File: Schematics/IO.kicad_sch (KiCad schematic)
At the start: 1 part

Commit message: BOM + Motor Controllers
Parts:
- added R?: 0R, symbol Device:R_Small_US
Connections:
- net Earth: now also R?.2
- net at J?.4 (ID): now also R?.1
- no-connect marks 1 -> 0
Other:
- note added: "NL"
- moved on the sheet: J?
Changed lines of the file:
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@@
 (kicad_sch (version 20211123) (generator eeschema)
   (paper "A4")
-  (junction (at 64.135 73.66) (diameter 0) (color 0 0 0 0)
+  (junction (at 70.485 73.025) (diameter 0) (color 0 0 0 0)
   )
-  (no_connect (at 74.295 66.04))
-  (wire (pts (xy 74.295 55.88) (xy 81.28 55.88))
+  (wire (pts (xy 80.645 55.245) (xy 87.63 55.245))
     (stroke (width 0) (type default) (color 0 0 0 0))
   )
-  (wire (pts (xy 74.295 60.96) (xy 81.28 60.96))
+  (wire (pts (xy 80.645 65.405) (xy 83.82 65.405))
     (stroke (width 0) (type default) (color 0 0 0 0))
   )
-  (wire (pts (xy 64.135 73.66) (xy 64.135 71.12))
+  (wire (pts (xy 80.645 60.325) (xy 87.63 60.325))
     (stroke (width 0) (type default) (color 0 0 0 0))
   )
-  (wire (pts (xy 64.135 76.2) (xy 64.135 73.66))
+  (wire (pts (xy 70.485 73.025) (xy 70.485 70.485))
     (stroke (width 0) (type default) (color 0 0 0 0))
   )
-  (wire (pts (xy 64.135 73.66) (xy 66.675 73.66))
+  (wire (pts (xy 70.485 75.565) (xy 70.485 73.025))
     (stroke (width 0) (type default) (color 0 0 0 0))
   )
-  (wire (pts (xy 74.295 63.5) (xy 81.28 63.5))
+  (wire (pts (xy 83.82 73.66) (xy 83.82 75.565))
     (stroke (width 0) (type default) (color 0 0 0 0))
   )
-  (wire (pts (xy 66.675 73.66) (xy 66.675 71.12))
+  (wire (pts (xy 83.82 65.405) (xy 83.82 68.58))
     (stroke (width 0) (type default) (color 0 0 0 0))
   )
-  (global_label "D+" (shape input) (at 81.28 60.96 0) (fields_autoplaced)
+  (wire (pts (xy 70.485 73.025) (xy 73.025 73.025))
+    (stroke (width 0) (type default) (color 0 0 0 0))
+  )
+  (wire (pts (xy 80.645 62.865) (xy 87.63 62.865))
+    (stroke (width 0) (type default) (color 0 0 0 0))
+  )
+  (wire (pts (xy 73.025 73.025) (xy 73.025 70.485))
+    (stroke (width 0) (type default) (color 0 0 0 0))
+  )
+  (text "NL" (at 86.36 75.565 0)
+    (effects (font (size 1.27 1.27)) (justify left bottom))
+  )
+  (global_label "D+" (shape input) (at 87.63 60.325 0) (fields_autoplaced)
     (effects (font (size 1.27 1.27)) (justify left))
-    (property "Intersheet References" "${INTERSHEET_REFS}" (id 0) (at 86.5355 60.8806 0)
+    (property "Intersheet References" "${INTERSHEET_REFS}" (id 0) (at 92.8855 60.2456 0)
       (effects (font (size 1.27 1.27)) (justify left) hide)
     )
   )
-  (global_label "VBUS" (shape input) (at 81.28 55.88 0) (fields_autoplaced)
+  (global_label "VBUS" (shape input) (at 87.63 55.245 0) (fields_autoplaced)
     (effects (font (size 1.27 1.27)) (justify left))
-    (property "Intersheet References" "${INTERSHEET_REFS}" (id 0) (at 88.5917 55.8006 0)
+    (property "Intersheet References" "${INTERSHEET_REFS}" (id 0) (at 94.9417 55.1656 0)
       (effects (font (size 1.27 1.27)) (justify left) hide)
     )
   )
-  (global_label "D-" (shape input) (at 81.28 63.5 0) (fields_autoplaced)
+  (global_label "D-" (shape input) (at 87.63 62.865 0) (fields_autoplaced)
     (effects (font (size 1.27 1.27)) (justify left))
-    (property "Intersheet References" "${INTERSHEET_REFS}" (id 0) (at 86.5355 63.4206 0)
+    (property "Intersheet References" "${INTERSHEET_REFS}" (id 0) (at 92.8855 62.7856 0)
       (effects (font (size 1.27 1.27)) (justify left) hide)
     )
   )
-  (symbol (lib_id "Connector:USB_B_Micro") (at 66.675 60.96 0) (unit 1)
+  (symbol (lib_id "Device:R_Small_US") (at 83.82 71.12 0) (unit 1)
     (in_bom yes) (on_board yes) (fields_autoplaced)
-    (property "Reference" "J?" (id 0) (at 66.675 48.26 0))
-    (property "Value" "USB_B_Micro" (id 1) (at 66.675 50.8 0))
-    (property "Footprint" "" (id 2) (at 70.485 62.23 0)
+    (property "Reference" "R?" (id 0) (at 86.36 69.8499 0)
+      (effects (font (size 1.27 1.27)) (justify left))
+    )
+    (property "Value" "0R" (id 1) (at 86.36 72.3899 0)
+      (effects (font (size 1.27 1.27)) (justify left))
+    )
+    (property "Footprint" "" (id 2) (at 83.82 71.12 0)
       (effects (font (size 1.27 1.27)) hide)
     )
-    (property "Datasheet" "~" (id 3) (at 70.485 62.23 0)
+    (property "Datasheet" "~" (id 3) (at 83.82 71.12 0)
+      (effects (font (size 1.27 1.27)) hide)
+    )
+    (pin "1")
+    (pin "2")
+  )
+  (symbol (lib_id "power:Earth") (at 83.82 75.565 0) (unit 1)
+    (in_bom yes) (on_board yes) (fields_autoplaced)
+    (property "Reference" "#PWR?" (id 0) (at 83.82 81.915 0)
+      (effects (font (size 1.27 1.27)) hide)
+    )
+    (property "Value" "Earth" (id 1) (at 83.82 79.375 0)
+      (effects (font (size 1.27 1.27)) hide)
+    )
+    (property "Footprint" "" (id 2) (at 83.82 75.565 0)
+      (effects (font (size 1.27 1.27)) hide)
+    )
+    (property "Datasheet" "~" (id 3) (at 83.82 75.565 0)
+      (effects (font (size 1.27 1.27)) hide)
+    )
+    (pin "1")
+  )
+  (symbol (lib_id "Connector:USB_B_Micro") (at 73.025 60.325 0) (unit 1)
+    (in_bom yes) (on_board yes) (fields_autoplaced)
+    (property "Reference" "J?" (id 0) (at 73.025 47.625 0))
+    (property "Value" "USB_B_Micro" (id 1) (at 73.025 50.165 0))
+    (property "Footprint" "" (id 2) (at 76.835 61.595 0)
+      (effects (font (size 1.27 1.27)) hide)
+    )
+    (property "Datasheet" "~" (id 3) (at 76.835 61.595 0)
       (effects (font (size 1.27 1.27)) hide)
     )
@@
     (pin "6")
   )
-  (symbol (lib_id "power:Earth") (at 64.135 76.2 0) (unit 1)
+  (symbol (lib_id "power:Earth") (at 70.485 75.565 0) (unit 1)
     (in_bom yes) (on_board yes) (fields_autoplaced)
-    (property "Reference" "#PWR?" (id 0) (at 64.135 82.55 0)
+    (property "Reference" "#PWR?" (id 0) (at 70.485 81.915 0)
       (effects (font (size 1.27 1.27)) hide)
     )
-    (property "Value" "Earth" (id 1) (at 64.135 80.01 0)
+    (property "Value" "Earth" (id 1) (at 70.485 79.375 0)
       (effects (font (size 1.27 1.27)) hide)
     )
-    (property "Footprint" "" (id 2) (at 64.135 76.2 0)
+    (property "Footprint" "" (id 2) (at 70.485 75.565 0)
       (effects (font (size 1.27 1.27)) hide)
     )
-    (property "Datasheet" "~" (id 3) (at 64.135 76.2 0)
+    (property "Datasheet" "~" (id 3) (at 70.485 75.565 0)
       (effects (font (size 1.27 1.27)) hide)
     )

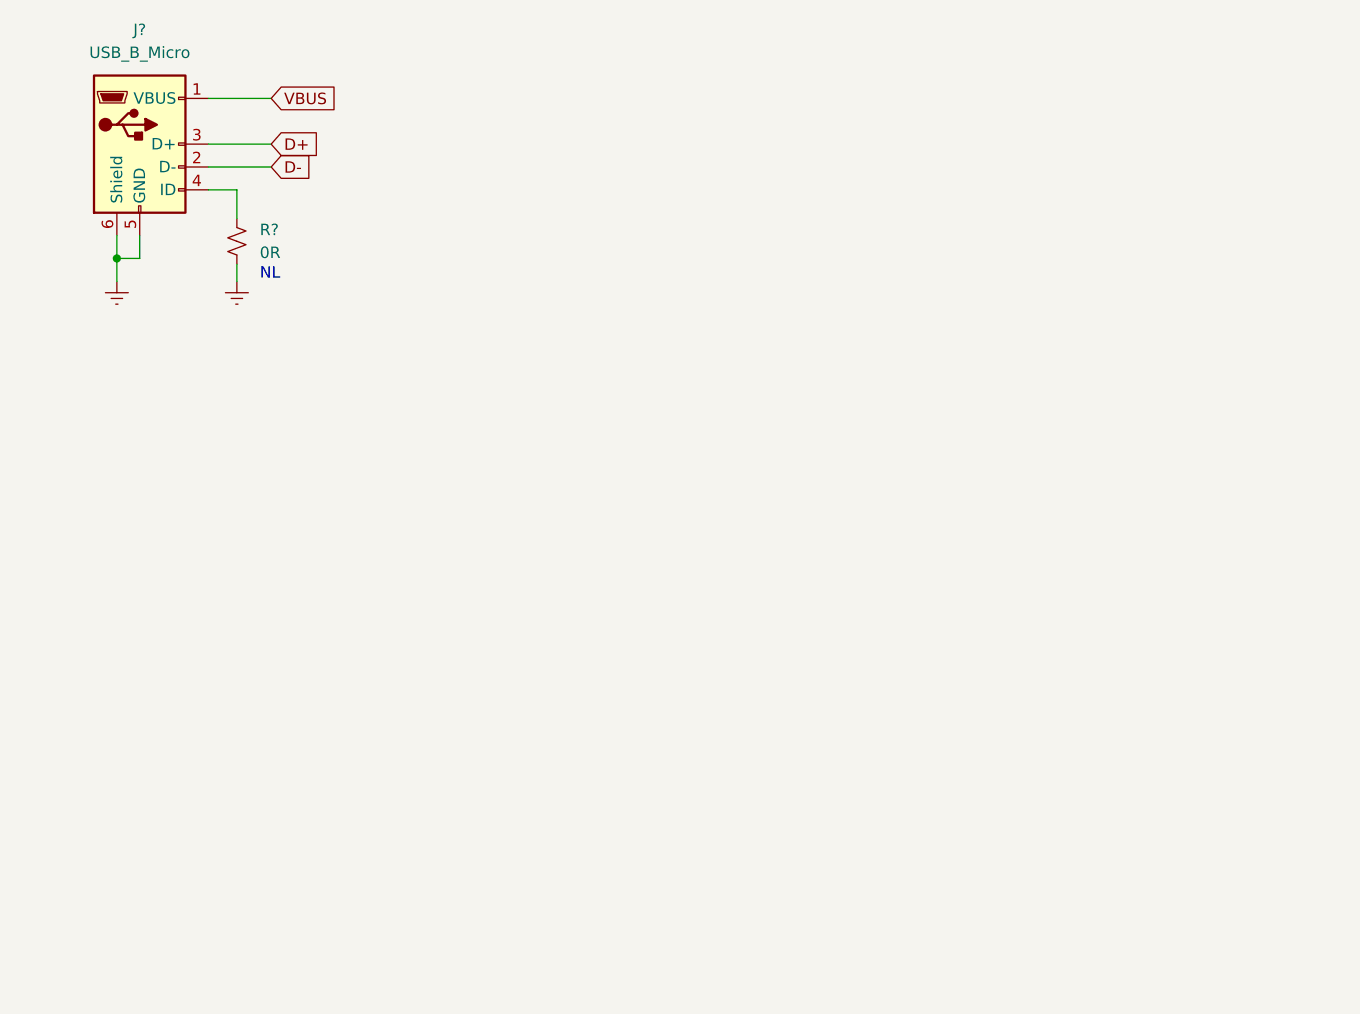
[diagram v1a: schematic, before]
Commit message: Changed MCU
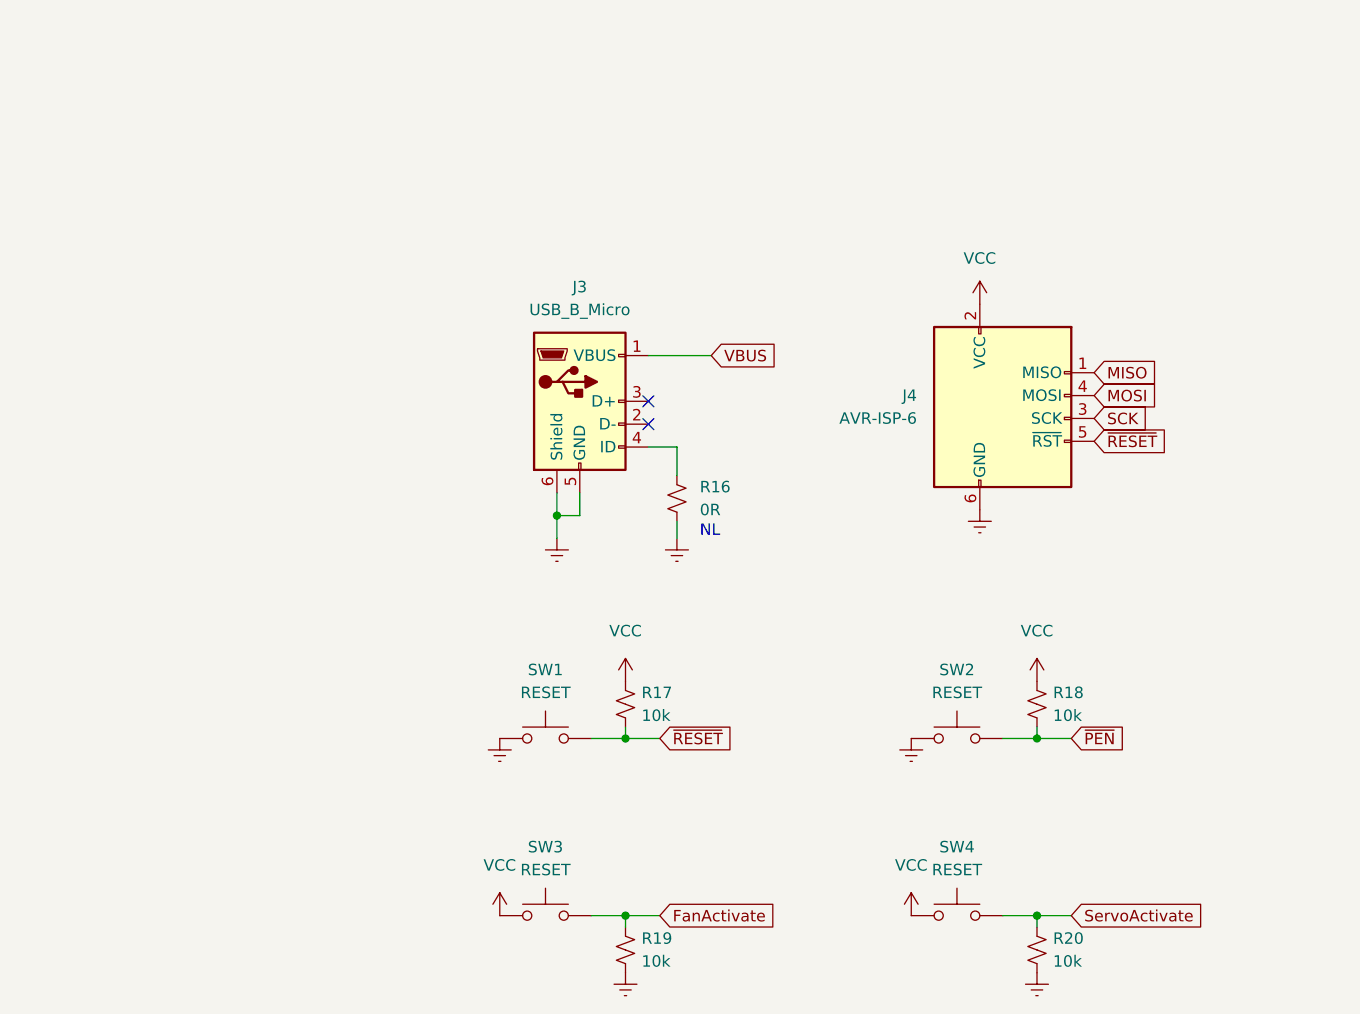
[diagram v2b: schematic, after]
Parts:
- added J4: AVR-ISP-6, symbol Connector:AVR-ISP-6
- added R17, R18, R19, R20: 10k, symbol Device:R_Small_US
- added SW1, SW2, SW3, SW4: RESET, symbol Switch:SW_MEC_5G
- gave numbers to parts that had none: 2
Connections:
- net Earth: now also J4.6 (GND), R19.2, R20.2, SW1.1 (A), SW1.2 (A), SW2.1 (A), SW2.2 (A)
- net D+: no longer names the net of J3.3 (D+)
- net D-: no longer names the net of J3.2 (D-)
- new net FanActivate: R19.1, SW3.3 (B), SW3.4 (B)
- new net MISO: J4.1 (MISO)
- new net MOSI: J4.4 (MOSI)
- new net SCK: J4.3 (SCK)
- new net ServoActivate: R20.1, SW4.3 (B), SW4.4 (B)
- new net VCC: J4.2 (VCC), R17.1, R18.1, SW3.1 (A), SW3.2 (A), SW4.1 (A), SW4.2 (A)
- new net ~{PEN}: R18.2, SW2.3 (B), SW2.4 (B)
- new net ~{RESET}: J4.5 (~{RST}), R17.2, SW1.3 (B), SW1.4 (B)
- no-connect marks 0 -> 2
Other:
- moved on the sheet: J3, R16

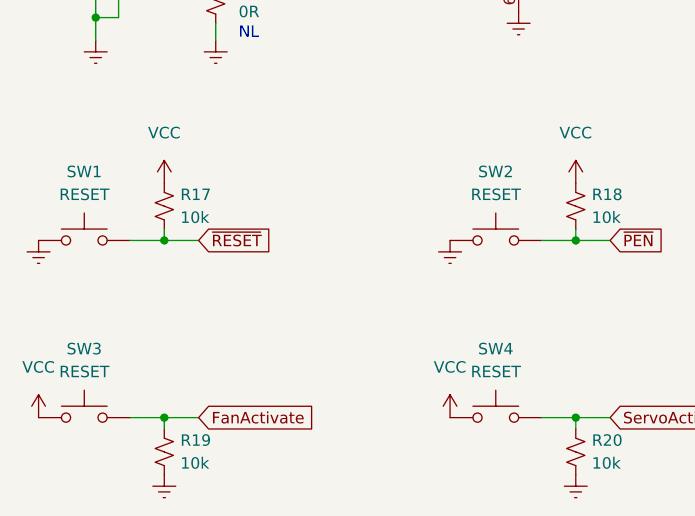
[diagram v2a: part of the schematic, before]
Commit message: Added Footprints
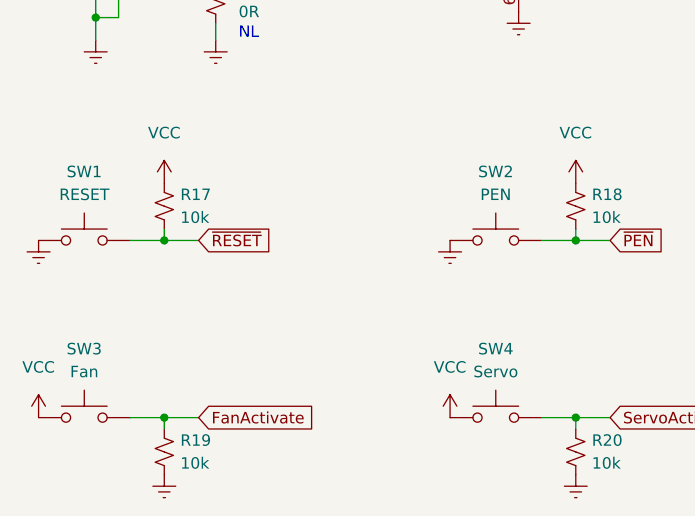
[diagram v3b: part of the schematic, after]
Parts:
- J3: footprint (none) -> SFRFootprints:MOLEX_105164-0001
- J4: footprint (none) -> SFRFootprints:TSW-103-08-F-D-RA
- R16, R17, R18, R19, R20: footprint (none) -> Resistor_SMD:R_0603_1608Metric_Pad0.98x0.95mm_HandSolder
- SW1: footprint (none) -> SFRFootprints:R-667843
- SW2: value RESET -> PEN; footprint (none) -> SFRFootprints:R-667843
- SW3: value RESET -> Fan; footprint (none) -> SFRFootprints:R-667843
- SW4: value RESET -> Servo; footprint (none) -> SFRFootprints:R-667843
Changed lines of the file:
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@@
     (in_bom yes) (on_board yes) (fields_autoplaced)
     (property "Reference" "SW2" (id 0) (at 163.83 118.745 0))
-    (property "Value" "RESET" (id 1) (at 163.83 121.285 0))
-    (property "Footprint" "" (id 2) (at 163.83 121.285 0)
+    (property "Value" "PEN" (id 1) (at 163.83 121.285 0))
+    (property "Footprint" "SFRFootprints:R-667843" (id 2) (at 163.83 121.285 0)
       (effects (font (size 1.27 1.27)) hide)
     )
@@
       (effects (font (size 1.27 1.27)) (justify left))
     )
-    (property "Footprint" "" (id 2) (at 172.72 149.86 0)
+    (property "Footprint" "Resistor_SMD:R_0603_1608Metric_Pad0.98x0.95mm_HandSolder" (id 2) (at 172.72 149.86 0)
       (effects (font (size 1.27 1.27)) hide)
     )
@@
       (effects (font (size 1.27 1.27)) (justify left))
     )
-    (property "Footprint" "" (id 2) (at 132.715 99.695 0)
+    (property "Footprint" "Resistor_SMD:R_0603_1608Metric_Pad0.98x0.95mm_HandSolder" (id 2) (at 132.715 99.695 0)
       (effects (font (size 1.27 1.27)) hide)
     )
@@
       (effects (font (size 1.27 1.27)) (justify left))
     )
-    (property "Footprint" "" (id 2) (at 127 149.86 0)
+    (property "Footprint" "Resistor_SMD:R_0603_1608Metric_Pad0.98x0.95mm_HandSolder" (id 2) (at 127 149.86 0)
       (effects (font (size 1.27 1.27)) hide)
     )
@@
       (effects (font (size 1.27 1.27)) (justify right))
     )
-    (property "Footprint" "" (id 2) (at 162.56 89.535 90)
+    (property "Footprint" "SFRFootprints:TSW-103-08-F-D-RA" (id 2) (at 162.56 89.535 90)
       (effects (font (size 1.27 1.27)) hide)
     )
@@
     (in_bom yes) (on_board yes) (fields_autoplaced)
     (property "Reference" "SW4" (id 0) (at 163.83 138.43 0))
-    (property "Value" "RESET" (id 1) (at 163.83 140.97 0))
-    (property "Footprint" "" (id 2) (at 163.83 140.97 0)
+    (property "Value" "Servo" (id 1) (at 163.83 140.97 0))
+    (property "Footprint" "SFRFootprints:R-667843" (id 2) (at 163.83 140.97 0)
       (effects (font (size 1.27 1.27)) hide)
     )
@@
     (property "Reference" "J3" (id 0) (at 121.92 76.2 0))
     (property "Value" "USB_B_Micro" (id 1) (at 121.92 78.74 0))
-    (property "Footprint" "" (id 2) (at 125.73 90.17 0)
+    (property "Footprint" "SFRFootprints:MOLEX_105164-0001" (id 2) (at 125.73 90.17 0)
       (effects (font (size 1.27 1.27)) hide)
     )
@@
     (in_bom yes) (on_board yes) (fields_autoplaced)
     (property "Reference" "SW3" (id 0) (at 118.11 138.43 0))
-    (property "Value" "RESET" (id 1) (at 118.11 140.97 0))
-    (property "Footprint" "" (id 2) (at 118.11 140.97 0)
+    (property "Value" "Fan" (id 1) (at 118.11 140.97 0))
+    (property "Footprint" "SFRFootprints:R-667843" (id 2) (at 118.11 140.97 0)
       (effects (font (size 1.27 1.27)) hide)
     )
@@
     (property "Reference" "SW1" (id 0) (at 118.11 118.745 0))
     (property "Value" "RESET" (id 1) (at 118.11 121.285 0))
-    (property "Footprint" "" (id 2) (at 118.11 121.285 0)
+    (property "Footprint" "SFRFootprints:R-667843" (id 2) (at 118.11 121.285 0)
       (effects (font (size 1.27 1.27)) hide)
     )
@@
       (effects (font (size 1.27 1.27)) (justify left))
     )
-    (property "Footprint" "" (id 2) (at 127 122.555 0)
+    (property "Footprint" "Resistor_SMD:R_0603_1608Metric_Pad0.98x0.95mm_HandSolder" (id 2) (at 127 122.555 0)
       (effects (font (size 1.27 1.27)) hide)
     )
@@
       (effects (font (size 1.27 1.27)) (justify left))
     )
-    (property "Footprint" "" (id 2) (at 172.72 122.555 0)
-      (effects (font (size 1.27 1.27)) hide)
-    )
+    (property "Footprint" "Resistor_SMD:R_0603_1608Metric_Pad0.98x0.95mm_HandSolder" (id 2) (at 172.72 122.555 0)
+      (effects (font (size 1.27 1.27)) hide)
+    )

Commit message: PCB
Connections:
- net FanActivate: now also SW3.2 (A); no longer SW3.3 (B)
- net ServoActivate: now also SW4.2 (A); no longer SW4.3 (B)
- net ~{PEN}: now also SW2.2 (A); no longer SW2.3 (B)
- net ~{RESET}: now also SW1.2 (A); no longer SW1.3 (B)
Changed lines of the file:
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@@
   (junction (at 119.38 101.6) (diameter 0) (color 0 0 0 0)
   )
+  (junction (at 172.72 126.365) (diameter 0) (color 0 0 0 0)
+  )
+  (junction (at 127 146.05) (diameter 0) (color 0 0 0 0)
+  )
   (junction (at 127 126.365) (diameter 0) (color 0 0 0 0)
   )
-  (junction (at 127 146.05) (diameter 0) (color 0 0 0 0)
-  )
   (junction (at 172.72 146.05) (diameter 0) (color 0 0 0 0)
-  )
-  (junction (at 172.72 126.365) (diameter 0) (color 0 0 0 0)
   )
   (no_connect (at 129.54 91.44))
@@
     (stroke (width 0) (type default) (color 0 0 0 0))
   )
+  (wire (pts (xy 123.19 126.365) (xy 127 126.365))
+    (stroke (width 0) (type default) (color 0 0 0 0))
+  )
   (wire (pts (xy 127 125.095) (xy 127 126.365))
     (stroke (width 0) (type default) (color 0 0 0 0))
@@
   )
   (wire (pts (xy 127 146.05) (xy 130.81 146.05))
-    (stroke (width 0) (type default) (color 0 0 0 0))
-  )
-  (wire (pts (xy 123.19 126.365) (xy 127 126.365))
     (stroke (width 0) (type default) (color 0 0 0 0))
   )
@@
     )
   )
-  (symbol (lib_id "Switch:SW_MEC_5G") (at 163.83 126.365 0) (unit 1)
+  (symbol (lib_name "SW_MEC_5G_3") (lib_id "Switch:SW_MEC_5G") (at 163.83 126.365 0) (unit 1)
     (in_bom yes) (on_board yes) (fields_autoplaced)
     (property "Reference" "SW2" (id 0) (at 163.83 118.745 0))
@@
     )
     (pin "1")
-    (pin "3")
+    (pin "2")
     (pin "2")
     (pin "4")
@@
     )
     (pin "1")
-    (pin "3")
+    (pin "2")
     (pin "2")
     (pin "4")
@@
     (pin "1")
   )
-  (symbol (lib_id "Switch:SW_MEC_5G") (at 118.11 146.05 0) (unit 1)
+  (symbol (lib_name "SW_MEC_5G_1") (lib_id "Switch:SW_MEC_5G") (at 118.11 146.05 0) (unit 1)
     (in_bom yes) (on_board yes) (fields_autoplaced)
     (property "Reference" "SW3" (id 0) (at 118.11 138.43 0))
@@
     )
     (pin "1")
-    (pin "3")
-    (pin "2")
-    (pin "4")
-  )
-  (symbol (lib_id "Switch:SW_MEC_5G") (at 118.11 126.365 0) (unit 1)
+    (pin "2")
+    (pin "2")
+    (pin "4")
+  )
+  (symbol (lib_name "SW_MEC_5G_2") (lib_id "Switch:SW_MEC_5G") (at 118.11 126.365 0) (unit 1)
     (in_bom yes) (on_board yes) (fields_autoplaced)
     (property "Reference" "SW1" (id 0) (at 118.11 118.745 0))
@@
     )
     (pin "1")
-    (pin "3")
-    (pin "2")
-    (pin "4")
+    (pin "2")
+    (pin "2")
+    (pin "4")

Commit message: PCB
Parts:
- SW1: value RESET -> Rest
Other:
- moved on the sheet: R17
